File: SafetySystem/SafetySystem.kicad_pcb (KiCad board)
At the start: 2 copper layers, 70 x 60 mm, 84 parts, among them J1 Screw_Terminal_01x02, J10 Screw_Terminal_01x02, J2 Screw_Terminal_01x02, J3 Screw_Terminal_01x02, J4 AVR-ISP-10, J5 Screw_Terminal_01x02, J6 Screw_Terminal_01x02, J7 Screw_Terminal_01x02, J8 Screw_Terminal_01x02, J9 Screw_Terminal_01x02, Q1 Q_PMOS_GSD, Q10 Q_NMOS_GSD, Q11 Q_NMOS_GSD, Q12 Q_NMOS_GSD, Q2 Q_PMOS_GSD, Q3 Q_PMOS_GSD, Q4 Q_NMOS_GSD, Q5 Q_NMOS_GSD, Q6 Q_NMOS_GSD, Q7 Q_NMOS_GSD, Q8 Q_NMOS_GSD, Q9 Q_NMOS_GSD, SW2 SW_Push, SW3 SW_Push, SW4 SW_Push, U1 ST1S10PHR, U2 MQ-8, U3 ATmega8A-AU, U4 LTV-817S, U5 LTV-817S, Y1 8Mhz

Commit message: Minor changes.
Squashed commit of the following:

commit b4817053897282ec246551fcbd580ae102a3b469
Author: Paweł <mackipawel@gmail.com>
Date:   Thu Apr 25 22:57:44 2019 +0200

    Minor changes.
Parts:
- added G***: LOGO, Footprints:EcoTech_small, F.Cu at (220.2, 104.8)
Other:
- board text added: "INV"
- board text added: "RST"
- board text added: "SEM"

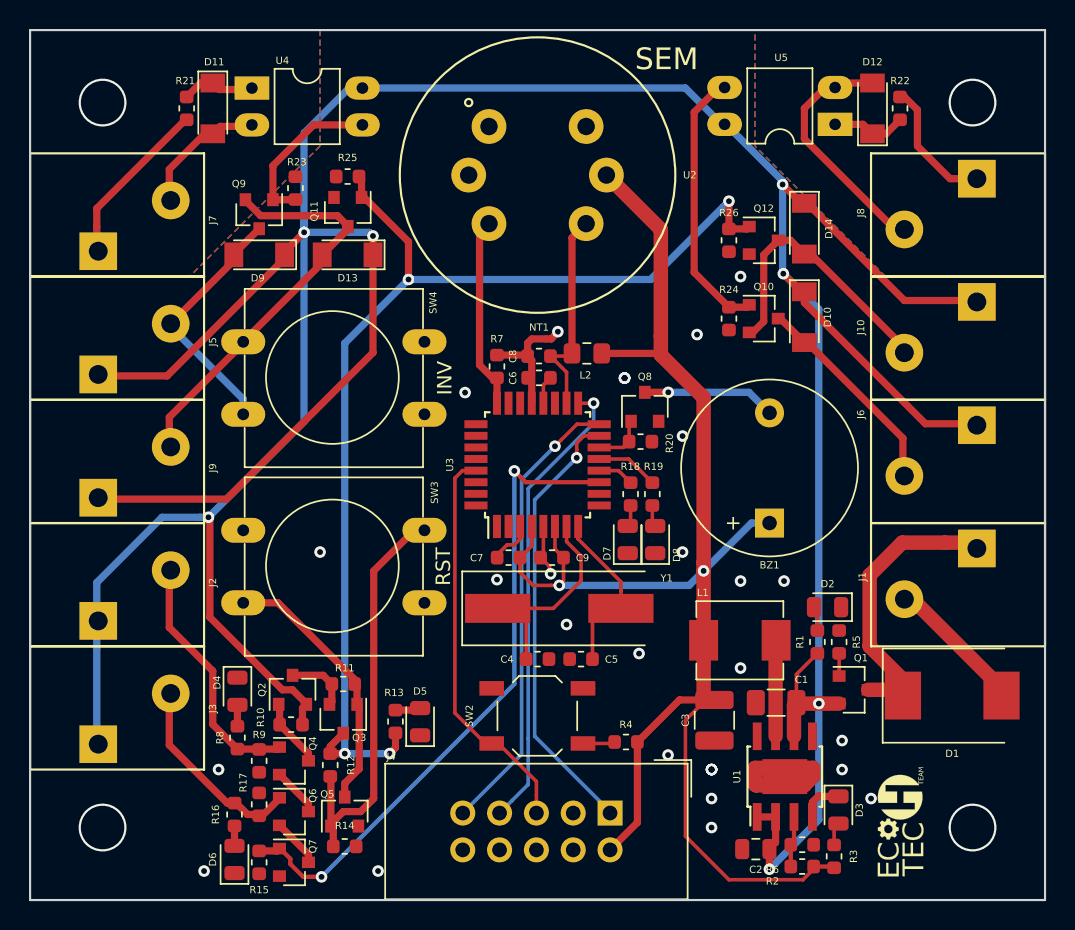
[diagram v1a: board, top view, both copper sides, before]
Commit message: SafetySystem potentiometer.
Squashed commit of the following:

commit c85b31eae362b98e5e9037a9aad6a815148d0818
Author: Paweł <mackipawel@gmail.com>
Date:   Sun Apr 28 12:07:02 2019 +0200

    Added potentiometer to the SafetySysytem.
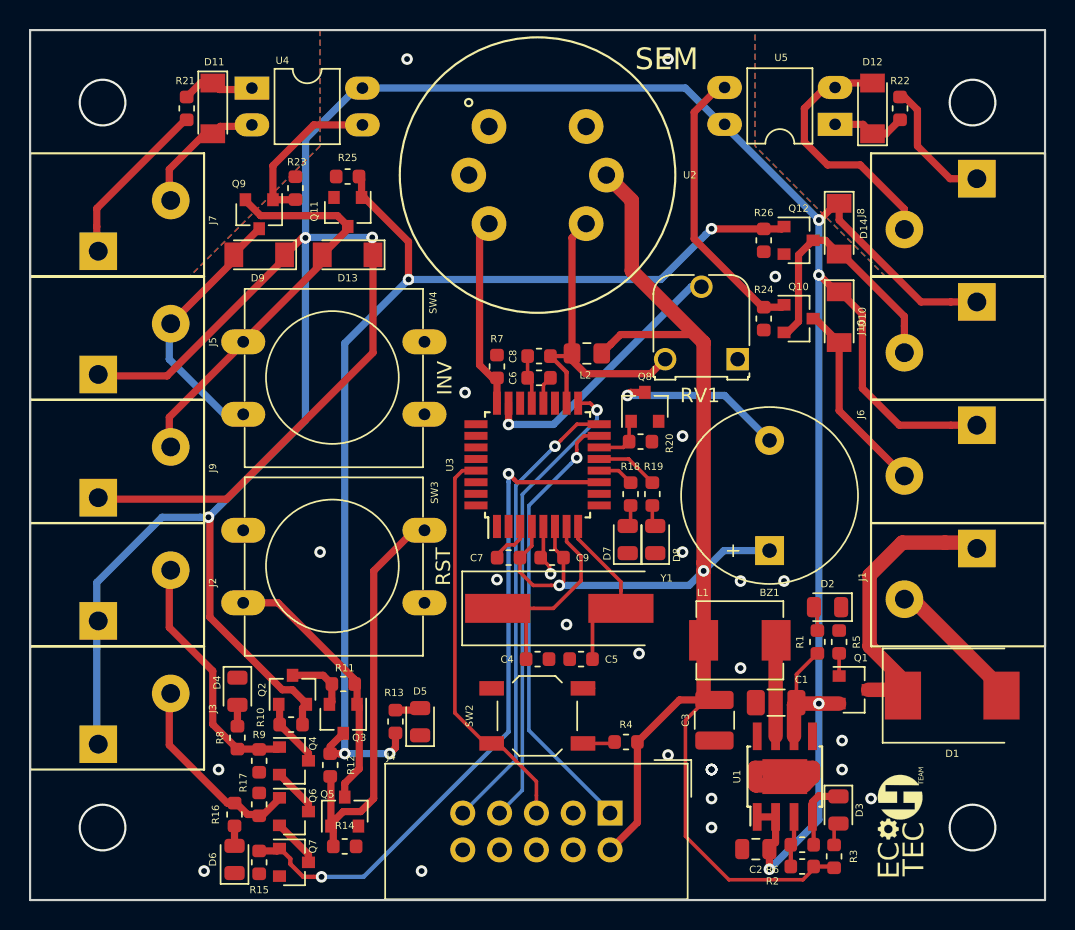
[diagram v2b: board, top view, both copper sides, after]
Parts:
- removed NT1: Net-Tie_2, NetTie:NetTie-2_SMD_Pad0.5mm
- added RV1: 10k, Potentiometer_THT:Potentiometer_Runtron_RM-065_Vertical, F.Cu at (208.8, 72.7)
- G1: renamed from G***; value LOGO -> EcoTechLogo
- moved D10 2.40 mm to (215.8, 69.8)
- moved D14 2.40 mm to (215.8, 63.7)
- moved Q10 2.40 mm to (213.0, 69.9)
- moved Q12 2.40 mm to (213.0, 64.5)
- moved R24 2.40 mm to (210.6, 69.9)
- moved R26 2.40 mm to (210.6, 64.5)
- moved BZ1 1.90 mm to (211.0, 85.9)
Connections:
- C6 pad 2: GNDA -> GND
- C8 pad 2: GNDA -> GND
- R7 pad 2: GNDA -> GND
- U3 pad 21: GNDA -> GND
- U3 pad 23: Net-(U3-Pad23) -> /ADC_POT
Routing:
- net /ADC_POT: track 0.00 -> 18.7 mm, vias 0 -> 1
- net GNDA: track 7.73 -> 0.00 mm
- net +5VA: track 14.6 -> 22.3 mm
- net GND: track 28.5 -> 33.4 mm, vias 29 -> 26
- net Net-(BZ1-Pad2): track 9.19 -> 12.4 mm
- net +12V: track 259.5 -> 256.5 mm
- net +5V: track 107.1 -> 110.0 mm
- net /H2_SIG: track 45.1 -> 46.7 mm
- net Net-(Q10-Pad1): track 18.7 -> 19.8 mm
- net Net-(D12-Pad2): track 17.0 -> 18.0 mm
- net Net-(D10-Pad2): track 14.5 -> 13.7 mm
- net /INLET: track 17.1 -> 17.8 mm
- net Net-(D14-Pad2): track 19.5 -> 18.7 mm

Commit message: Removed Switches from bus devices and added mounting holes in schematics.
Squashed commit of the following:

commit 448b4f84a5f64686dc4334a0b6d81609891ca7cf
Author: Paweł <mackipawel@gmail.com>
Date:   Sun Apr 28 20:22:14 2019 +0200

    Added mouting holes to SystemSupply.

commit d45917b7024ecbe087cb8328a2c33d3ab10399ff
Author: Paweł <mackipawel@gmail.com>
Date:   Sun Apr 28 20:13:41 2019 +0200

    Added mouting holes to SafetySystem.

commit 6365380671305e2241dc821ec3b00ae08a997ac5
Author: Paweł <mackipawel@gmail.com>
Date:   Sun Apr 28 20:11:13 2019 +0200

    Added mouting holes to SafetySupply.

commit 00163d4bba61eb48f9ebb4c601b04017e78006be
Author: Paweł <mackipawel@gmail.com>
Date:   Sun Apr 28 20:06:38 2019 +0200

    Fixed MotorController.

commit ec0507ca51ef80aebbe2605505e7109beac59e98
Author: Paweł <mackipawel@gmail.com>
Date:   Sun Apr 28 19:54:40 2019 +0200

    Fixed MotorDriver.
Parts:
- added H1: MountingHole, MountingHole:MountingHole_3.2mm_M3, F.Cu at (225.0, 55.0)
- added H2: MountingHole, MountingHole:MountingHole_3.2mm_M3, F.Cu at (225.0, 105.0)
- added H3: MountingHole, MountingHole:MountingHole_3.2mm_M3, F.Cu at (165.0, 105.0)
- added H4: MountingHole, MountingHole:MountingHole_3.2mm_M3, F.Cu at (165.0, 55.0)
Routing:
- net (no net): vias 4 -> 0

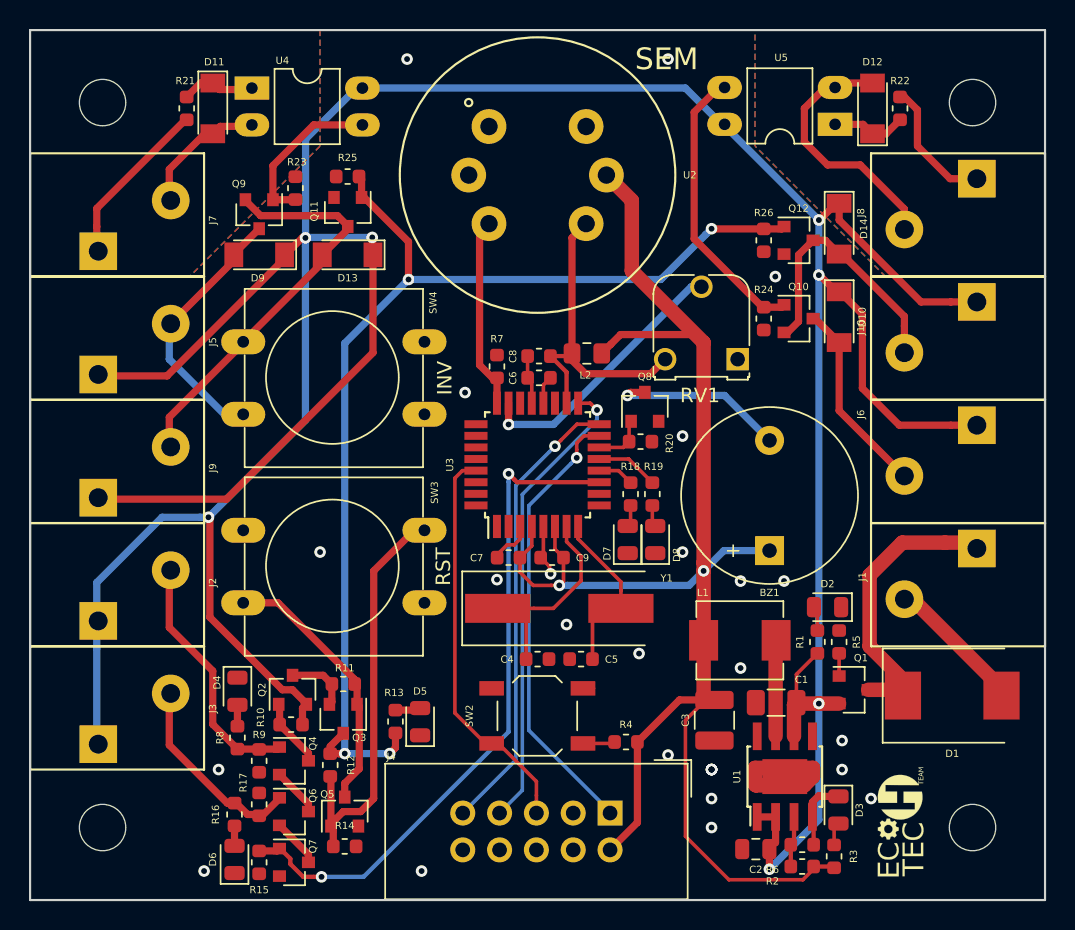
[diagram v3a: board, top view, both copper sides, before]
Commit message: Added testpoints.
Squashed commit of the following:

commit b78741095f1293168643ce5f943c13a7eb09b318
Author: Paweł <mackipawel@gmail.com>
Date:   Thu May 2 10:22:35 2019 +0200

    Added testpoints to remaining projects.

commit d708f3fd02ddff10684a41533d76b9b66ea6c8f4
Author: Paweł <mackipawel@gmail.com>
Date:   Sun Apr 28 23:49:47 2019 +0200

    Added testpoints in MotorController and MotorDriver.
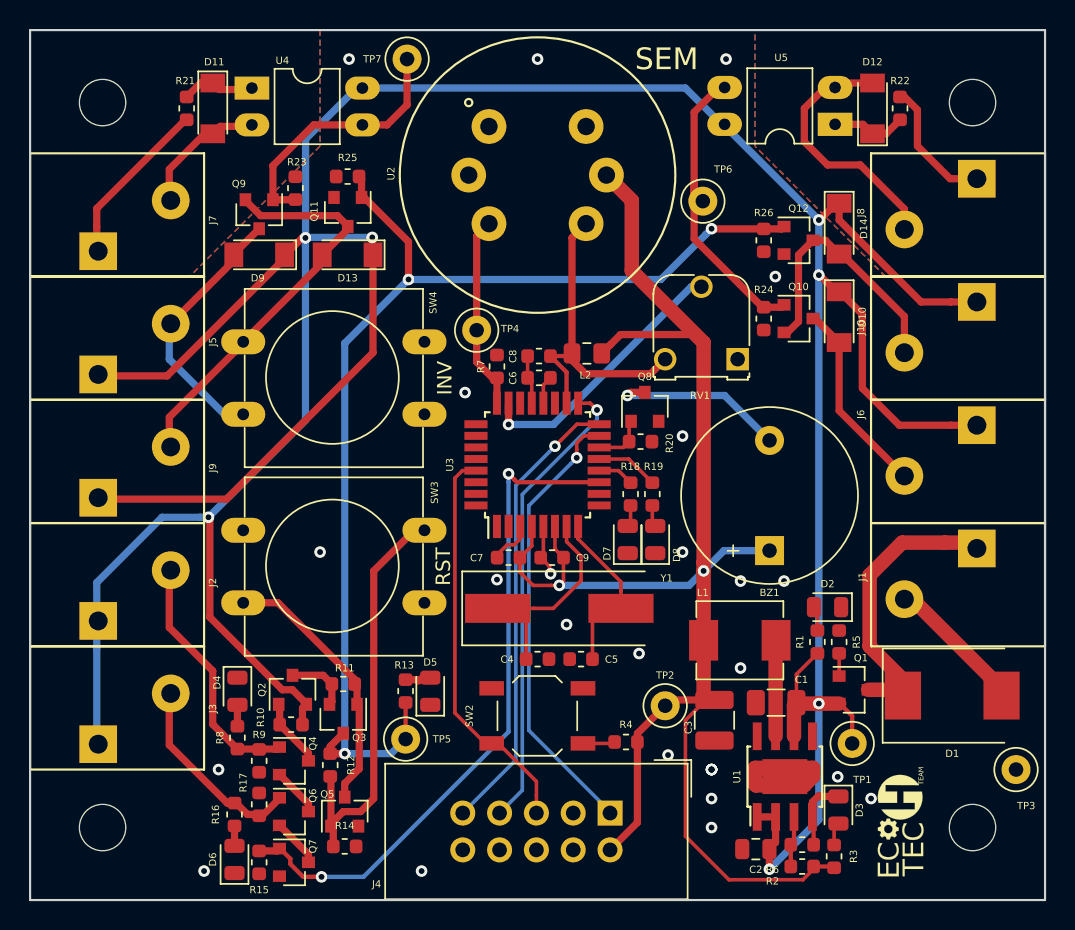
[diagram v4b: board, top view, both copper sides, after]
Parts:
- added TP1: TestPoint, TestPoint:TestPoint_Loop_D1.80mm_Drill1.0mm_Beaded, F.Cu at (216.7, 99.2)
- added TP2: TestPoint, TestPoint:TestPoint_Loop_D1.80mm_Drill1.0mm_Beaded, F.Cu at (203.8, 96.6)
- added TP3: TestPoint, TestPoint:TestPoint_Loop_D1.80mm_Drill1.0mm_Beaded, F.Cu at (228.0, 101.0)
- added TP4: TestPoint, TestPoint:TestPoint_Loop_D1.80mm_Drill1.0mm_Beaded, F.Cu at (190.8, 70.7)
- added TP5: TestPoint, TestPoint:TestPoint_Loop_D1.80mm_Drill1.0mm_Beaded, F.Cu at (185.9, 98.9)
- added TP6: TestPoint, TestPoint:TestPoint_Loop_D1.80mm_Drill1.0mm_Beaded, F.Cu at (206.4, 61.8)
- added TP7: TestPoint, TestPoint:TestPoint_Loop_D1.80mm_Drill1.0mm_Beaded, F.Cu at (186.0, 52.0)
- moved D5 2.21 mm to (187.6, 95.6)
- moved R13 2.21 mm to (185.9, 95.6)
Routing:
- net Net-(Q9-Pad1): track 11.4 -> 18.2 mm
- net +12V: track 256.5 -> 259.7 mm
- net /SFT_SIG: track 78.7 -> 80.9 mm, vias 4 -> 3
- net Net-(Q10-Pad1): track 19.8 -> 21.2 mm

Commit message: Added 3D models to the library
Squashed commit of the following:

commit 8070c09fc3d8f70a7cb84d0f12b6782c2c87c14c
Author: Paweł <mackipawel@gmail.com>
Date:   Mon May 6 20:26:56 2019 +0200

    Added SystemSupply 3d models.

commit 94ef8708632c7bc91211bc6ded4e0c8fb9ccef4a
Author: Paweł <mackipawel@gmail.com>
Date:   Mon May 6 01:08:52 2019 +0200

    Added 3D models to SystemSupply.

commit eb394d70be979be958e4acab21accb1817e8e0e5
Author: Paweł <mackipawel@gmail.com>
Date:   Mon May 6 00:55:39 2019 +0200

    Added 3D model to MotorController.

commit fd89e01e0ef36f85afad3e8686d3deffdf36454d
Author: Paweł <mackipawel@gmail.com>
Date:   Mon May 6 00:40:56 2019 +0200

    Added 3D models in MotorDriver.

commit 899d106fa8d45578189a4955328047d8f9558beb
Author: Paweł <mackipawel@gmail.com>
Date:   Mon May 6 00:09:40 2019 +0200

    Added 3D models to SafetySupply.

commit 06c807994bb47431d2802a96796741a0e8fb9ae5
Author: Paweł <mackipawel@gmail.com>
Date:   Sun May 5 23:17:48 2019 +0200

    Added 3D models to SafetySystem.
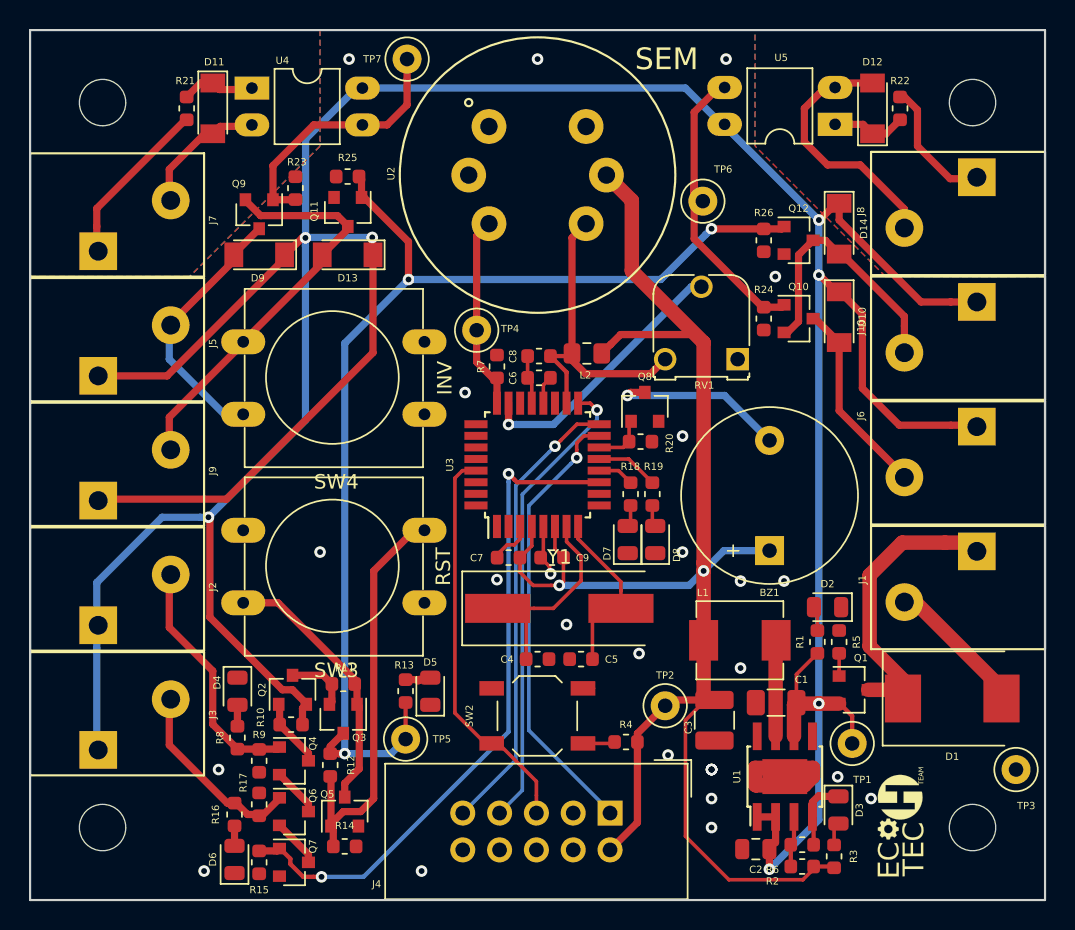
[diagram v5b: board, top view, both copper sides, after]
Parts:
- RV1: footprint Potentiometer_THT:Potentiometer_Runtron_RM-065_Vertical -> Footprints:Potentiometer_Runtron_RM-065_Vertical
- SW3, SW4: footprint Button_Switch_THT:SW_PUSH-12mm -> Footprints:SW_PUSH-12mm
- Y1: footprint Crystal:Crystal_SMD_HC49-SD -> Footprints:Crystal_SMD_HC49-SD
- moved J3 0.40 mm to (160.0, 101.4)
- moved J2 0.30 mm to (160.0, 92.8)
- moved J1 0.20 mm to (230.0, 84.2)
- moved J9 0.20 mm to (160.0, 84.2)
- moved D1 0.20 mm to (223.6, 96.1)
- moved J8 0.10 mm to (230.0, 58.4)
- moved J5 0.10 mm to (160.0, 75.6)
- moved J6 0.10 mm to (230.0, 75.6)

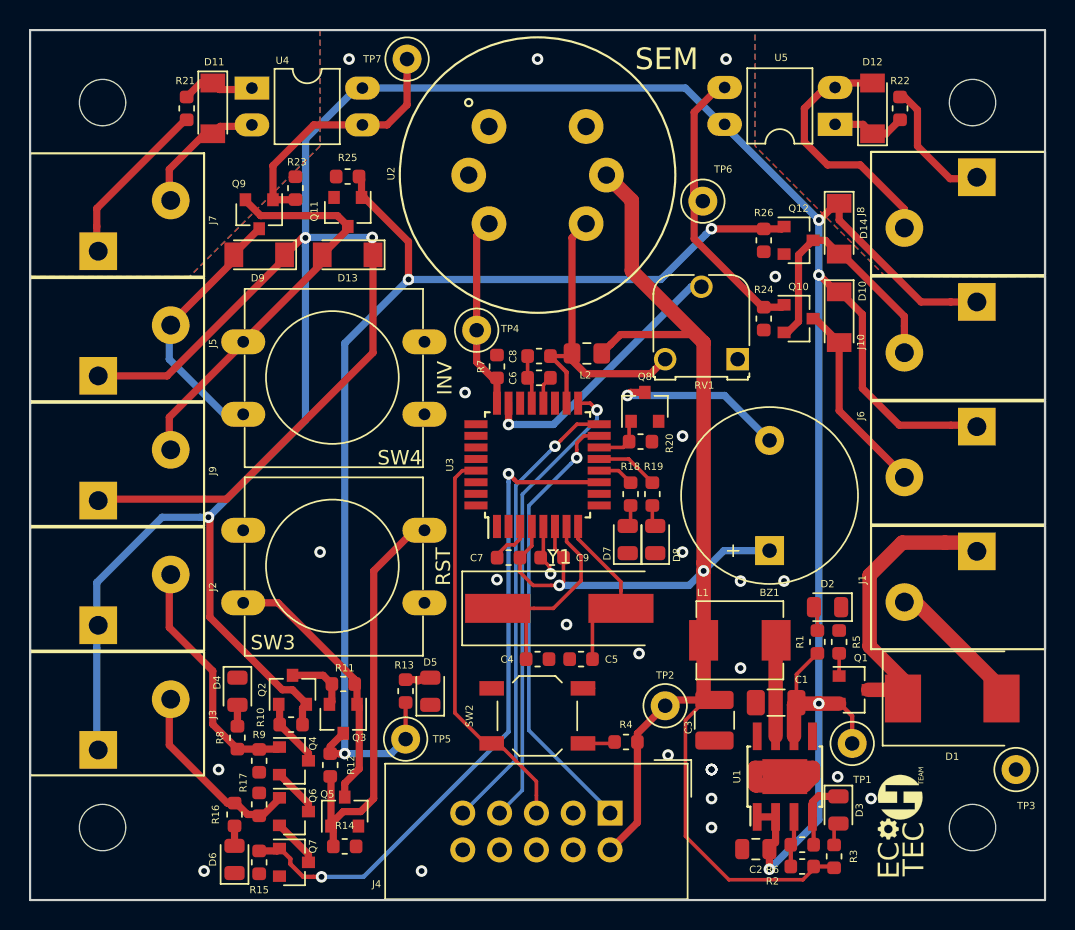
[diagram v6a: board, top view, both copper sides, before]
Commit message: Changed all via diameters to 0.7. Added project and version label on silk screen. Added more grounding vias.
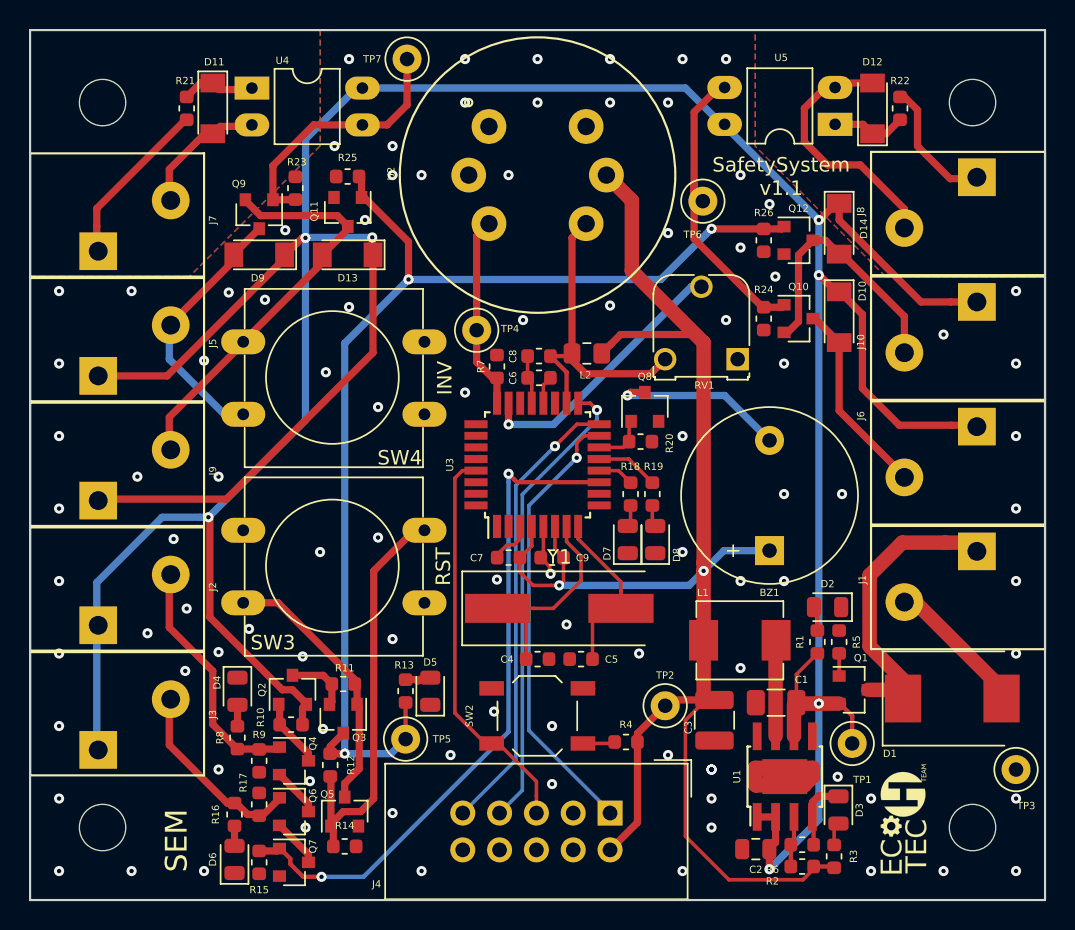
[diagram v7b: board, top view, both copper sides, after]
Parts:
- moved G1 0.28 mm to (220.4, 104.6)
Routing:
- net GND: vias 26 -> 98
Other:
- net class Default: via_dia 0.8 -> 0.7; via_drill 0.4 -> 0.3
- rule via_min_size: 0.4 -> 0.7
- board text added: "SafetySystem v1.1"
